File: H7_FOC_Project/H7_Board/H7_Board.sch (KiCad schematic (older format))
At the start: 49 parts

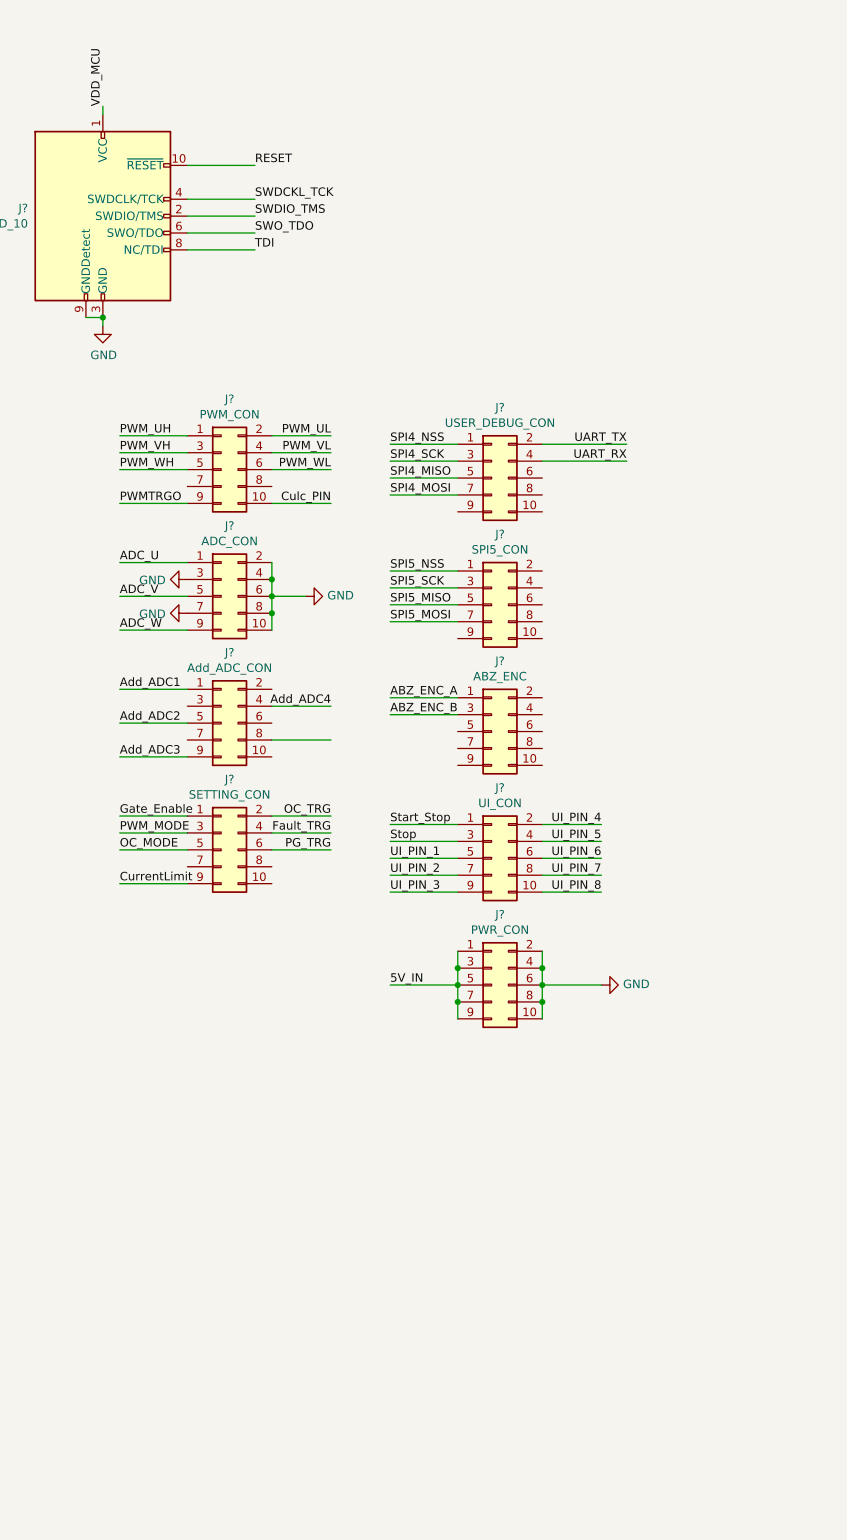
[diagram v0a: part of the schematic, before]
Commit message: [add] board schematic ESD
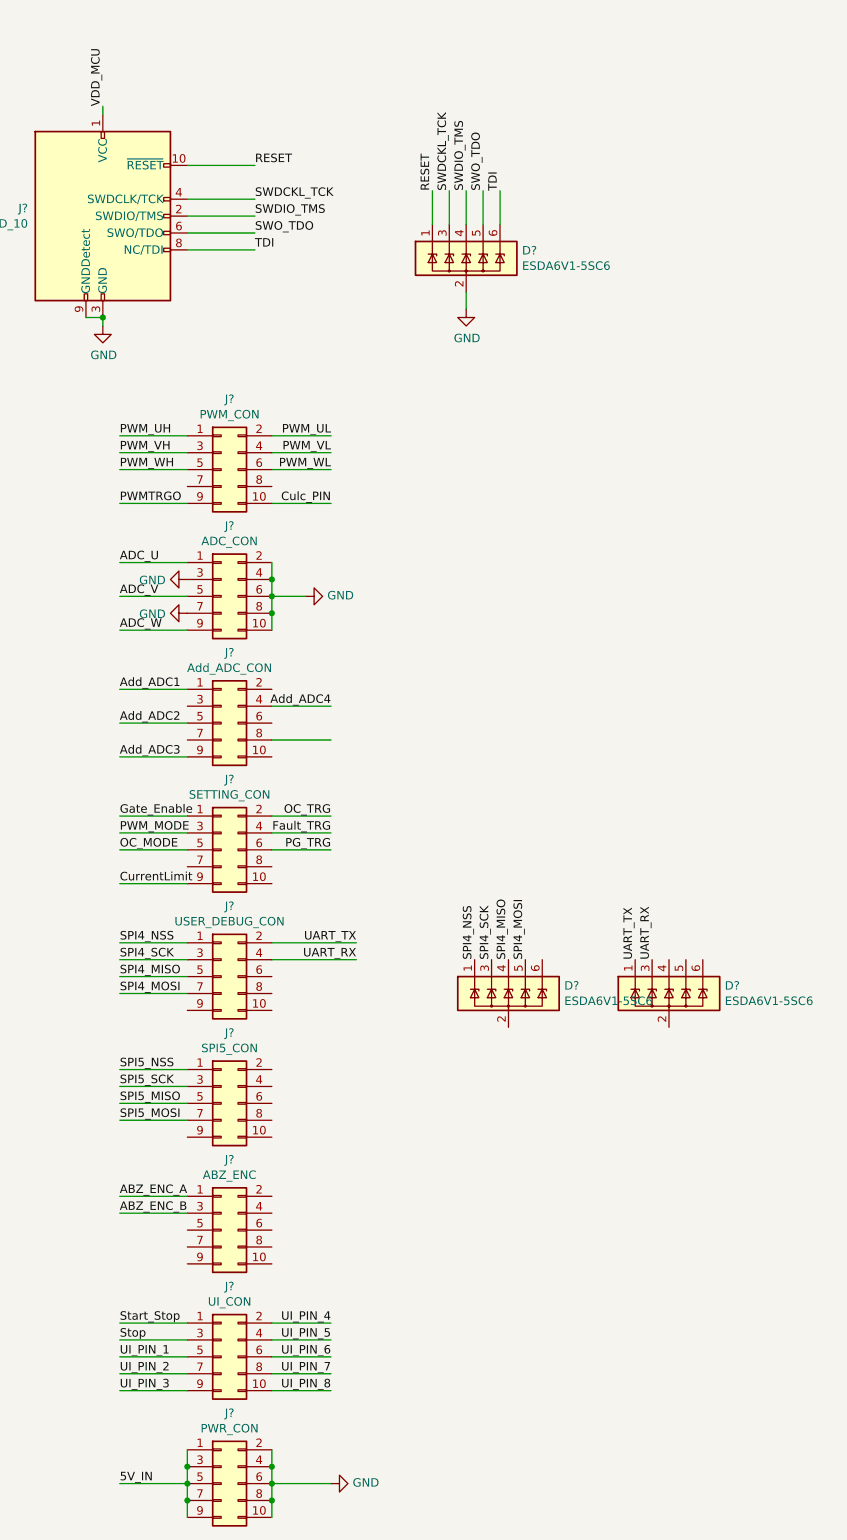
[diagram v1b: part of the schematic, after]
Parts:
- added D? (x3): ESDA6V1-5SC6, Package_TO_SOT_SMD:SOT-23-6, symbol Power_Protection:ESDA6V1-5SC6
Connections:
- net GND: now also D?.2 (GND)
- net RESET: now also D?.1 (IO1)
- net SPI4_MISO: now also D?.4 (IO3)
- net SPI4_MOSI: now also D?.5 (IO4)
- net SPI4_NSS: now also D?.1 (IO1)
- net SPI4_SCK: now also D?.3 (IO2)
- net SWDCKL_TCK: now also D?.3 (IO2)
- net SWDIO_TMS: now also D?.4 (IO3)
- net SWO_TDO: now also D?.5 (IO4)
- net TDI: now also D?.6 (IO5)
- net UART_RX: now also D?.3 (IO2)
- net UART_TX: now also D?.1 (IO1)
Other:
- moved on the sheet: J?

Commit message: [fix] board
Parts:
- removed JP?: SolderBridge, symbol Jumper:SolderJumper_2_Open
- added D1: D_ESD, Diode_SMD:D_MELF, symbol Device:D_Schottky_Small
- added D10, D11, D9: LED, LED_SMD:LED_0603_1608Metric, symbol Device:LED
- added D2, D4, D5, D8: ESDA6V1-5SC6, Package_TO_SOT_SMD:SOT-23-6, symbol Power_Protection:ESDA6V1-5SC6
- added JP1: SolderBridge, Jumper:SolderJumper-2_P1.3mm_Open_TrianglePad1.0x1.5mm, symbol Jumper:SolderJumper_2_Open
- added R5, R6, R7: 10k, Resistor_SMD:R_0603_1608Metric, symbol Device:R_Small
- C1, C10, C11, C12, C13, C14, C15, C16, C17, C18, C19, C2, C20, C21, C22, C23, C24, C25, C26, C27, C3, C4, C5, C6, C7, C9: renamed from C?; footprint (none) -> Capacitor_SMD:C_0603_1608Metric
- C8: renamed from C?; footprint (none) -> Capacitor_SMD:C_0805_2012Metric
- J10, J2, J3, J4, J5, J6, J7, J8, J9: renamed from J?; footprint (none) -> Connector_PinSocket_1.27mm:PinSocket_2x05_P1.27mm_Vertical_SMD
- JP2, JP3: renamed from JP?; footprint (none) -> Jumper:SolderJumper-2_P1.3mm_Open_TrianglePad1.0x1.5mm
- R1, R2, R3, R4: renamed from R?; footprint (none) -> Resistor_SMD:R_0603_1608Metric
- SW1: renamed from SW?; footprint (none) -> Button_Switch_SMD:SW_SPST_PTS810
- Y1, Y2: renamed from Y?; footprint (none) -> Crystal:Crystal_SMD_0603-4Pin_6.0x3.5mm
- gave numbers to parts that had none: 6
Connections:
- net 3V3_MCU is gone; now on net 3V3_VDD: JP2.1 (A)
- net AGND is gone; now on net GND: C12.2, C14.2, C15.2, C17.2, U2.31 (VSSA)
- net RESET is gone; now on net NJTRST: D6.1 (IO1), J1.10 (~RESET~)
- net 3V3_VDD: now also JP1.2 (B)
- net ABZ_ENC_A: now also D2.5 (IO4)
- net ABZ_ENC_B: now also D2.6 (IO5)
- net Fault_TRG: now also D2.3 (IO2)
- net GND: now also D3.2 (GND), D7.2 (GND), J2.7 (Pin_7), J2.8 (Pin_8), J4.10 (Pin_10), J4.2 (Pin_2), J4.3 (Pin_3), J4.6 (Pin_6), J4.7 (Pin_7), J4.8 (Pin_8), J5.10 (Pin_10), J5.7 (Pin_7), J5.8 (Pin_8), J6.6 (Pin_6), J6.9 (Pin_9), D1.2 (A), D2.2 (GND), D4.2 (GND), D5.2 (GND), D8.2 (GND), R5.2, R6.2, R7.2
- net LED1: now also D9.2 (A)
- net LED2: now also D10.2 (A)
- net LED3: now also D11.2 (A)
- net NRST: now also D1.1 (K)
- net OC_TRG: now also D2.4 (IO3)
- net PG_TRG: now also D2.1 (IO1)
- net SPI5_MISO: now also D4.4 (IO3)
- net SPI5_MOSI: now also D4.5 (IO4)
- net SPI5_NSS: now also D4.1 (IO1)
- net SPI5_SCK: now also D4.3 (IO2)
- net SWO_TDO: now also U2.133 (PB3); no longer U2.48 (PB2)
- net Start_Stop: now also D5.1 (IO1)
- net Stop: now also D5.3 (IO2)
- net UI_PIN_1: now also D5.4 (IO3); no longer U2.114 (PD0)
- net UI_PIN_2: now also D5.5 (IO4); no longer U2.115 (PD1)
- net UI_PIN_3: now also D5.6 (IO5)
- net UI_PIN_4: now also D8.1 (IO1)
- net UI_PIN_5: now also D8.3 (IO2)
- net UI_PIN_6: now also D8.4 (IO3)
- net UI_PIN_7: now also D8.5 (IO4)
- net UI_PIN_8: now also D8.6 (IO5)
- net VBAT: now also JP1.1 (A)
- net NJTRST: now reaches U2.134 (PB4)
- net CAN_RX: now reaches J6.10 (Pin_10)
- net CAN_RX: now also D7.6 (IO5), U2.114 (PD0)
- net CAN_TX: now reaches J6.8 (Pin_8)
- net CAN_TX: now also D7.5 (IO4), U2.115 (PD1)
- new net: D9.1 (K), R5.1
- new net: D10.1 (K), R6.1
- new net: D11.1 (K), R7.1
- no-connect marks 0 -> 75
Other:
- moved on the sheet: D3, D7, JP2, JP3

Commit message: [fix] schematic
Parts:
- removed J4: Add_ADC_CON, Connector_PinSocket_1.27mm:PinSocket_2x05_P1.27mm_Vertical_SMD, symbol Connector_Generic:Conn_02x05_Odd_Even
- removed J8: ABZ_ENC, Connector_PinSocket_1.27mm:PinSocket_2x05_P1.27mm_Vertical_SMD, symbol Connector_Generic:Conn_02x05_Odd_Even
- removed JP3: SolderBridge, Jumper:SolderJumper-2_P1.3mm_Open_TrianglePad1.0x1.5mm, symbol Jumper:SolderJumper_2_Open
- removed Y1: 8M, Crystal:Crystal_SMD_0603-4Pin_6.0x3.5mm, symbol Device:Crystal_GND23_Small
- removed Y2: 32K, Crystal:Crystal_SMD_0603-4Pin_6.0x3.5mm, symbol Device:Crystal_GND23_Small
- added D5, D6, D7: SBD, Diode_SMD:D_MELF, symbol Device:D_Schottky_Small
- added Y1: 8M RH100-8.000-20-3050-EXT-TR, Crystal:Crystal_SMD_3225-4Pin_3.2x2.5mm, symbol Device:Crystal_GND24_Small
- added Y2: 32k FC-135 32.7680KA-A0, Crystal:Crystal_SMD_3215-2Pin_3.2x1.5mm, symbol Device:Crystal
- C24, C25: value 5p -> 18p
- C26, C27: value 5p -> 12.5p
- J6: renamed from J7; value SPI5_CON -> ENC_CON
- renumbered D9 to D1, D4 to D10, D5 to D11, D6 to D12, D7 to D13, D8 to D14, D10 to D2, D11 to D3, D1 to D4, D2 to D8, D3 to D9, J5 to J4, J6 to J5, J10 to J7, J9 to J8, R5 to R3, R6 to R4, R7 to R5, R3 to R6, R4 to R7
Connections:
- net NRST is gone; now on net NJTRST: C21.1, D4.1 (K), SW1.2, U2.25 (NRST)
- net 3V3_VDD: now also D5.2 (A), D6.2 (A)
- net 5V_IN: now also D7.2 (A)
- net ABZ_ENC_A: now also J6.4 (Pin_4)
- net ABZ_ENC_B: now also J6.2 (Pin_2)
- net ADC_V: now also J3.3 (Pin_3); no longer J3.5 (Pin_5)
- net ADC_W: now also J3.5 (Pin_5); no longer J3.9 (Pin_9)
- net Add_ADC1: now also J3.7 (Pin_7)
- net Add_ADC2: now also J3.9 (Pin_9)
- net Add_ADC3: now also J3.2 (Pin_2)
- net Add_ADC4: now also J3.4 (Pin_4)
- net CAN_RX: now also J5.8 (Pin_8); no longer J5.10 (Pin_10)
- net CAN_TX: now also J5.6 (Pin_6); no longer J5.8 (Pin_8)
- net GND: now also J5.10 (Pin_10), J6.10 (Pin_10), Y1.2, Y1.4; no longer J3.2 (Pin_2), J3.3 (Pin_3), J3.4 (Pin_4), J3.7 (Pin_7), J5.6 (Pin_6), J5.9 (Pin_9)
- net VDDA: now also U2.33 (VDDA)
- net at C24.1, U2.23 (PH0): now also Y1.1
- net at C25.1, U2.24 (PH1): now also Y1.3
- net at C26.1, U2.8 (PC14): now also Y2.1
- net ABZ_ENC_GPIO: now reaches U2.85 (PD14)
- net ABZ_ENC_GPIO: now also J6.6 (Pin_6)
- net at C27.1, U2.9 (PC15): now also Y2.2
- net at J6.8 (Pin_8): now also D7.1 (K)
- net at J6.9 (Pin_9): now also D6.1 (K)
- new net: D5.1 (K), J5.9 (Pin_9)
- no-connect marks 75 -> 60
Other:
- moved on the sheet: J4, J5, J6, J7, J8

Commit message: [modify] CAD
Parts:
- removed D4: D_ESD, Diode_SMD:D_MELF, symbol Device:D_Schottky_Small
- added D4: ESDALC6V1-1U2, Diode_SMD:D_0201_0603Metric, symbol Device:D_TVS
- added R7: 10k, Resistor_SMD:R_0603_1608Metric, symbol Device:R_Small
- C1: renamed from C4; footprint Capacitor_SMD:C_0603_1608Metric -> Capacitor_SMD:C_0402_1005Metric
- C10: renamed from C20; footprint Capacitor_SMD:C_0603_1608Metric -> Capacitor_SMD:C_0402_1005Metric
- C12: footprint Capacitor_SMD:C_0603_1608Metric -> Capacitor_SMD:C_0402_1005Metric
- C14: renamed from C15; footprint Capacitor_SMD:C_0603_1608Metric -> Capacitor_SMD:C_0402_1005Metric
- C19: renamed from C2; footprint Capacitor_SMD:C_0603_1608Metric -> Capacitor_SMD:C_0402_1005Metric
- C2: renamed from C6; footprint Capacitor_SMD:C_0603_1608Metric -> Capacitor_SMD:C_0402_1005Metric
- C20: renamed from C5; footprint Capacitor_SMD:C_0603_1608Metric -> Capacitor_SMD:C_0402_1005Metric
- C23: renamed from C21; footprint Capacitor_SMD:C_0603_1608Metric -> Capacitor_SMD:C_0402_1005Metric
- C3: renamed from C7; footprint Capacitor_SMD:C_0603_1608Metric -> Capacitor_SMD:C_0402_1005Metric
- C4: renamed from C9; footprint Capacitor_SMD:C_0603_1608Metric -> Capacitor_SMD:C_0402_1005Metric
- C5: renamed from C10; footprint Capacitor_SMD:C_0603_1608Metric -> Capacitor_SMD:C_0402_1005Metric
- C6: renamed from C11; footprint Capacitor_SMD:C_0603_1608Metric -> Capacitor_SMD:C_0402_1005Metric
- C7: renamed from C13; footprint Capacitor_SMD:C_0603_1608Metric -> Capacitor_SMD:C_0402_1005Metric
- C8: renamed from C16; footprint Capacitor_SMD:C_0603_1608Metric -> Capacitor_SMD:C_0402_1005Metric
- C9: renamed from C18; footprint Capacitor_SMD:C_0603_1608Metric -> Capacitor_SMD:C_0402_1005Metric
- D5, D6, D7: value SBD -> SBD RB520S; footprint Diode_SMD:D_MELF -> Diode_SMD:D_0603_1608Metric
- SW1: value RST_SW -> SW_RESET
- renumbered C1 to C11, C14 to C13, C17 to C15, C19 to C16, C22 to C17, C23 to C18, C3 to C21, C8 to C22, R7 to R8
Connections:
- net 3V3_VDD: now also R7.1
- net BOOT0: now also R7.2
- net GND: now also D4.2 (A2)
- net NJTRST: now also D4.1 (A1)
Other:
- moved on the sheet: C1, C10, C11, C2, C3, C4, C5, C6, C7, C8, C9
